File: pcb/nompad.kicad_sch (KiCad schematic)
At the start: 40 parts, among them J1 Conn_01x02_Pin, SW1 ChocHS, SW10 ChocHS, SW11 ChocHS, SW12 ChocHS, SW13 ChocHS, SW14 ChocHS, SW15 ChocHS, SW16 ChocHS, SW17 ChocHS, SW18 ChocHS, SW2 ChocHS, SW3 ChocHS, SW4 ChocHS, SW5 ChocHS, SW6 ChocHS, SW7 ChocHS, SW8 ChocHS, SW9 ChocHS

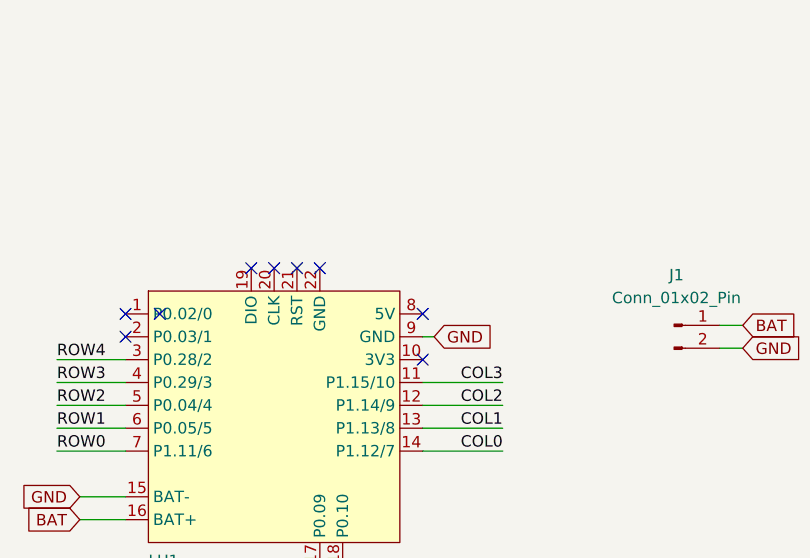
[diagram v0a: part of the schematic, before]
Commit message: Shrink PCB
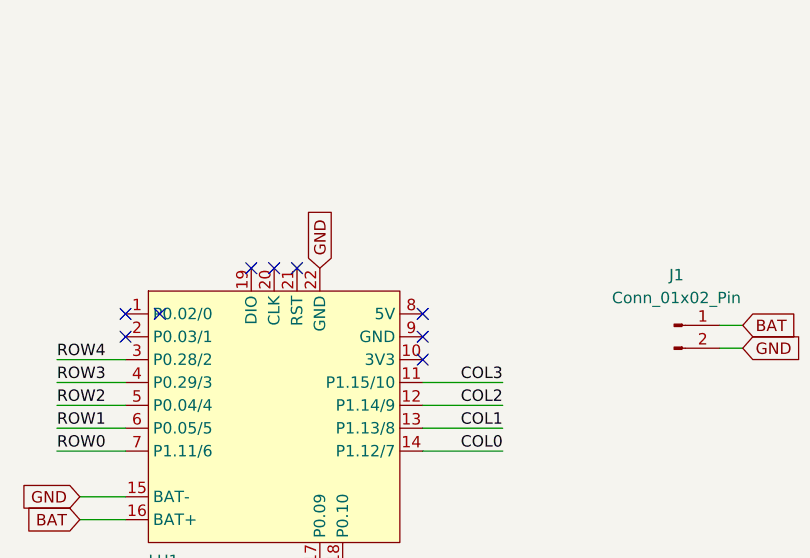
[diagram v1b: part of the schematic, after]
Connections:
- net GND: now also LU1.22 (GND); no longer LU1.9 (GND)
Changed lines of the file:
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@@
-	)
-	(no_connect
-		(at 185.42 82.55)
 	)
 	(no_connect
@@
 	)
 	(no_connect
+		(at 196.85 90.17)
+	)
+	(no_connect
 		(at 180.34 82.55)
 	)
@@
 	(wire
 		(pts
-			(xy 196.85 90.17) (xy 198.12 90.17)
-		)
-		(stroke
-			(width 0)
-			(type default)
-		)
-	)
-	(wire
-		(pts
 			(xy 82.55 105.41) (xy 82.55 125.73)
 		)
@@
 	(global_label "GND"
 		(shape input)
-		(at 198.12 90.17 0)
+		(at 185.42 82.55 90)
 		(fields_autoplaced yes)
 		(effects
@@
 		)
 		(property "Intersheetrefs" "${INTERSHEET_REFS}"
-			(at 206.0038 90.17 0)
+			(at 185.42 75.6943 90)
 			(effects
 				(font
